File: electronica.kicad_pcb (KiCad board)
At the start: 2 copper layers, 100 x 100 mm, 60 parts, among them J1 Conn_02x02_Counter_Clockwise, J2 Raspberry_Pi_4, J3 Conn_01x12, J4 Conn_01x05, P1 Conn_01x03_Socket, P2 Conn_01x03_Socket, P3 Conn_01x03_Socket, P4 Conn_01x03_Socket, U1 ADS1115 MOD, U2 ULN2003AID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

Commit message: agrege un conector de i2C a3.3v por lo que se ofresca
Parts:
- added I2C1: Conn_01x04, Connector_PinHeader_2.00mm:PinHeader_1x04_P2.00mm_Vertical, F.Cu at (53.5, 93.3)
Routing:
- net IO02-SDA: track 10.5 -> 46.3 mm
- net IO03-SCL: track 10.5 -> 46.0 mm
- net /3V3: track 91.3 -> 110.9 mm
- net Net-(J1-Pin_1): track 25.4 -> 26.2 mm
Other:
- board text added: "3.3V SDA SCL GND"

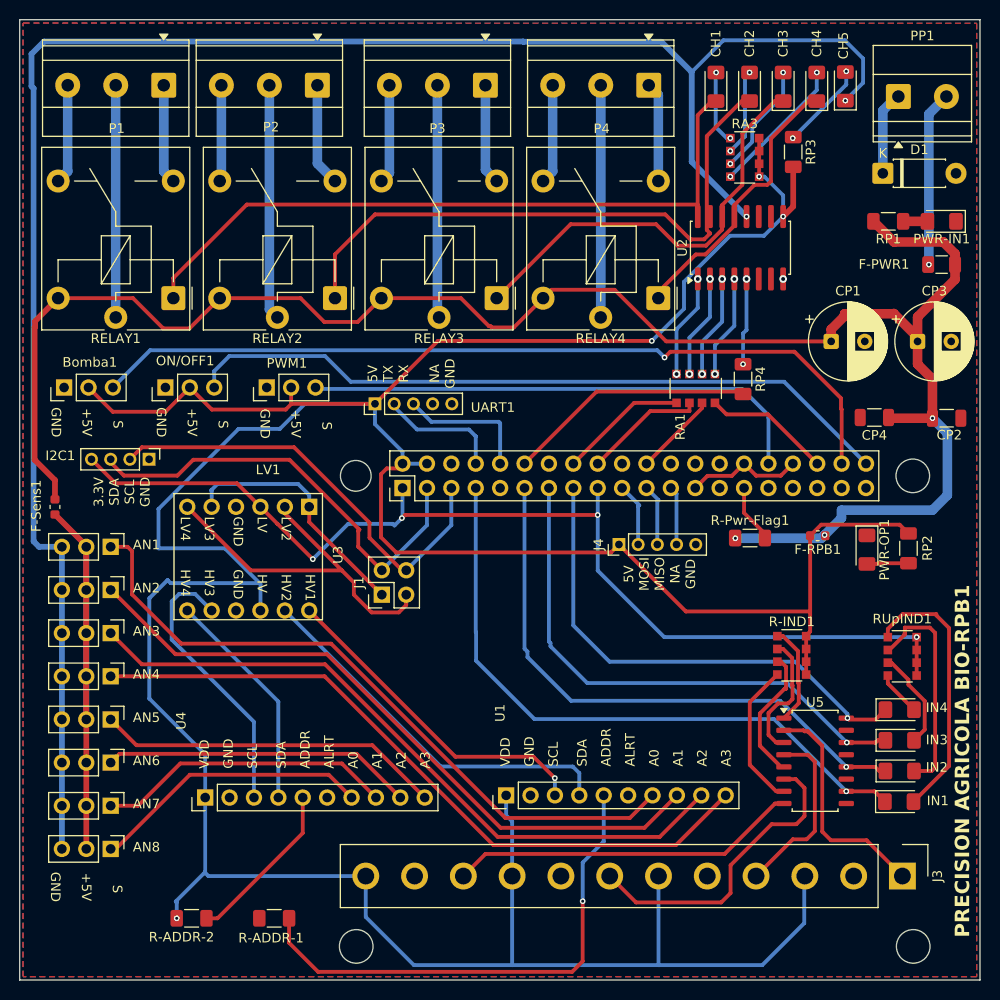
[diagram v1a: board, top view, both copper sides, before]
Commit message: movi las vias y optimice algunas rutas
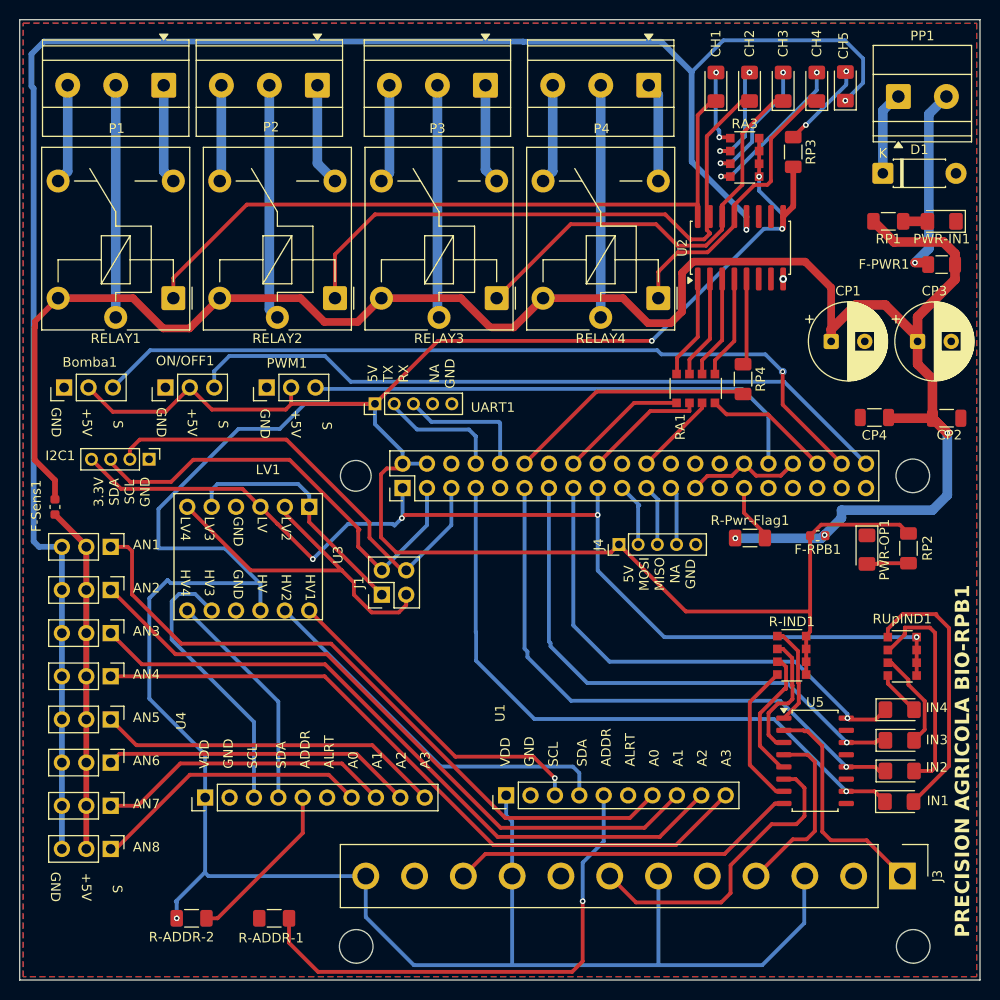
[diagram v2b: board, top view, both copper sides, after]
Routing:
- net /VIN: track 193.1 -> 205.7 mm
- net CONTROL SENORES: track 198.7 -> 201.4 mm
- net IO38: track 86.8 -> 84.4 mm
- net Net-(CH2-A): track 9.32 -> 11.5 mm
- net Net-(CH3-A): track 11.8 -> 13.8 mm
- net Net-(CH4-A): track 14.6 -> 16.5 mm
- net Net-(PP1-Pin_2): track 18.3 -> 20.1 mm
- net IO03-SCL: track 46.0 -> 47.3 mm
- net OUT4: track 29.2 -> 30.5 mm
- net IO02-SDA: track 46.3 -> 46.8 mm
- net Net-(RA1-R4.1): vias 2 -> 0
- net Net-(RA1-R1.1): vias 2 -> 0
- net Net-(U2-5B): vias 2 -> 0
- net Net-(RA1-R3.1): vias 2 -> 0
- net Net-(RA1-R2.1): vias 2 -> 0
